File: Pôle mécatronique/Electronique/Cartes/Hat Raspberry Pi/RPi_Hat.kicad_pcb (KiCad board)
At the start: 2 copper layers, 65 x 57.3 mm, 14 parts, among them J1 Conn_02x03_Odd_Even, J2 RPi_GPIO, U1 XBee, U2 MCP25625-x-SS, Y1 8MHz

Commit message: Update HAT + Commande
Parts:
- Y1: footprint Crystal:Crystal_HC49-U_Vertical -> Crystal:Crystal_HC50_Horizontal
- moved Y1 7.34 mm to (79.2, 77.9), turned to 0 degrees
- moved C3 1.91 mm to (73.7, 83.2)
- moved C4 1.91 mm to (90.2, 83.2)
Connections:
- Y1 pad 1: Net-(C4-Pad1) -> Net-(C3-Pad1)
- Y1 pad 2: Net-(C3-Pad1) -> Net-(C4-Pad1)
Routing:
- net GND: track 33.1 -> 53.5 mm
- net 3V3: track 104.8 -> 115.3 mm
- net /RPi_GPIO/BCM15_RXD: track 40.7 -> 50.9 mm
- net Net-(C3-Pad1): track 23.9 -> 13.9 mm
- net Net-(C4-Pad1): track 26.1 -> 16.4 mm
- net cmd_relais: track 31.9 -> 33.6 mm
- net can_L: track 11.8 -> 13.0 mm
- net 5VRPI: track 54.7 -> 53.9 mm
- net MOSI: track 33.7 -> 34.4 mm

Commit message: Résolution warning HAT
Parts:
- removed the ? at (121.7, 41.6)
- removed the ? at (63.7, 41.6)
- added ?: , , F.Cu at (66.5, 55.4)
- added ?: , , F.Cu at (87.9, 55.4)
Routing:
- net 5VRPI: track 53.9 -> 79.9 mm
- net Net-(C4-Pad1): track 16.4 -> 24.7 mm
- net Net-(C3-Pad1): track 13.9 -> 21.6 mm
- net 3V3: track 115.3 -> 109.6 mm
- net can_L: track 13.0 -> 12.5 mm

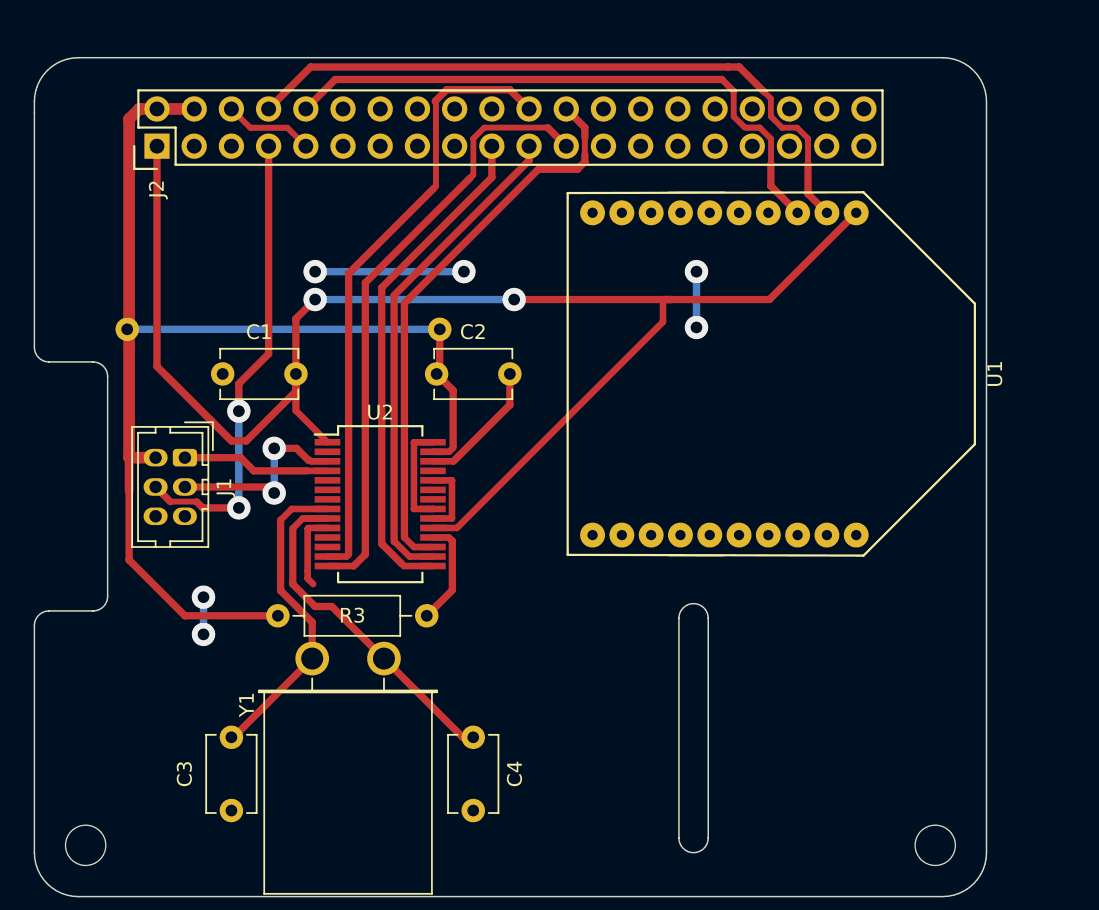
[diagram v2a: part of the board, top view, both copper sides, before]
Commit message: Résolution des problèmes du HAT
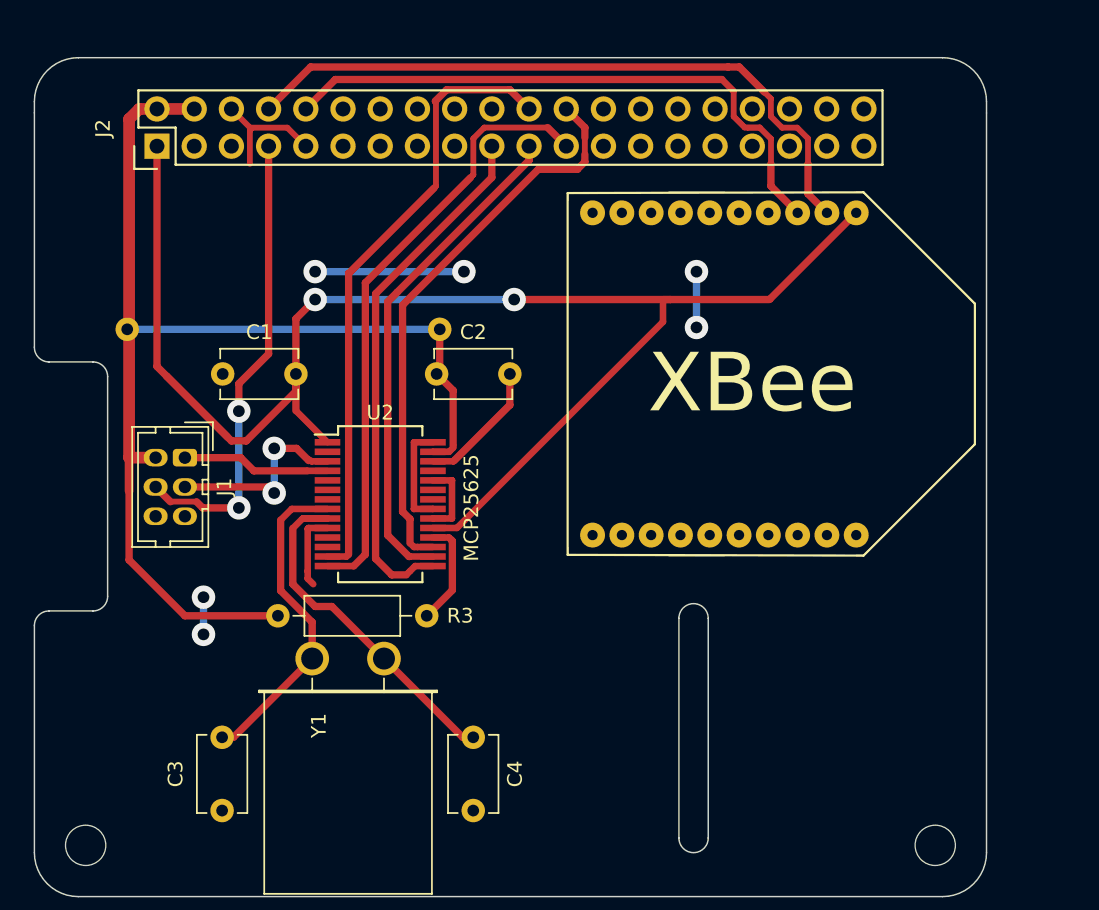
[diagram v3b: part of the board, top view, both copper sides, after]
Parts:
- U2: value MCP25625-x-SS -> MCP25625
- moved C3 0.63 mm to (73.0, 83.2)
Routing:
- net GND: track 53.1 -> 51.1 mm
- net MOSI: track 34.4 -> 36.1 mm
- net /RPi_GPIO/BCM15_RXD: track 50.9 -> 50.1 mm
- net Net-(C3-Pad1): track 21.6 -> 22.2 mm
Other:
- board text added: "XBee"

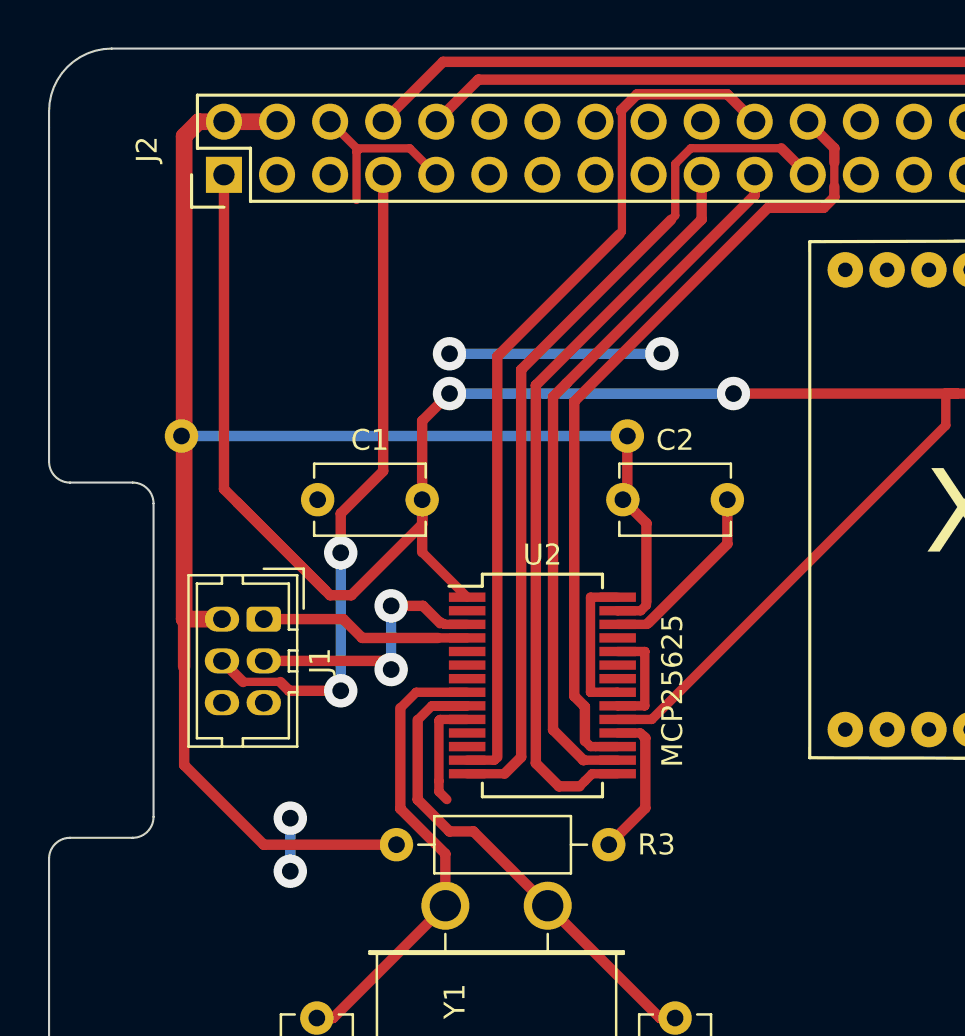
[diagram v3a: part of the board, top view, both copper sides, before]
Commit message: Update alim
Corrections pistes et via
Merci Hugo et Francois
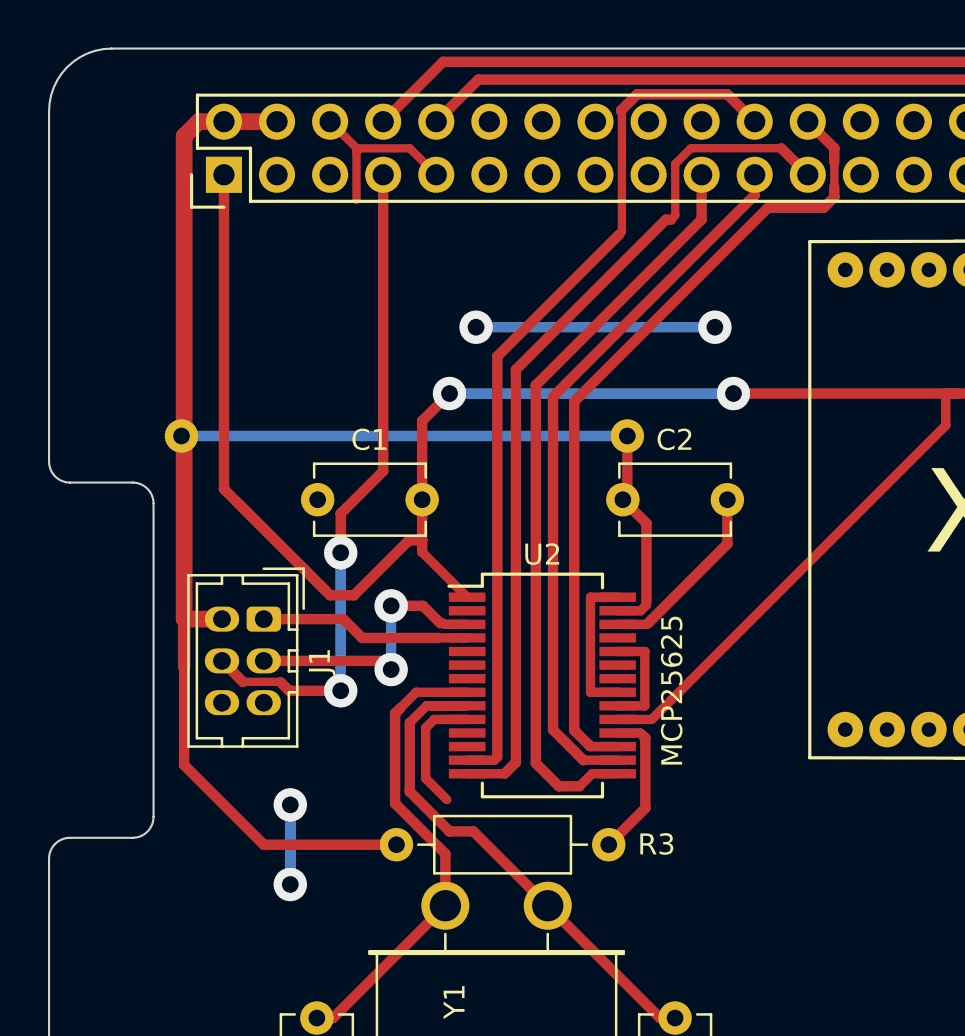
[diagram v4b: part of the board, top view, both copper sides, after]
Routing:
- net GND: track 51.1 -> 55.7 mm
- net 3V3: track 109.3 -> 107.8 mm
- net Net-(C4-Pad1): track 24.7 -> 25.3 mm
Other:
- board text removed: "Camera Flex Slot (Optional)"
- board text removed: "Dimensions taken from https://github.com/raspberrypi/hats/blob/master/hat-board-mechanical.pdf"
- board text removed: "Select one of these board edges depending upon the type of socket that is used."
